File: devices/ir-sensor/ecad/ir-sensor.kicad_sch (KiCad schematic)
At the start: 5 parts, among them J1 SM03B-SRSS-TB, U1 EE-SY1201

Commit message: Panelizes the IR Sensors
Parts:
- C1: MPN (none) -> CL10B103KB8NNNC; Manufacturer (none) -> Samsung Electro-Mechanics
- J1: MPN (none) -> SM03B-SRSS-TB; Manufacturer (none) -> JST
- R1: MPN (none) -> RC0603FR-07100L; Manufacturer (none) -> YAGEO
- R2: MPN (none) -> RC0603FR-07220L; Manufacturer (none) -> YAGEO
- U1: Manufacturer (none) -> Omron Electronics Inc
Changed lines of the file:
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@@
+			)
+		)
+		(property "MPN" "CL10B103KB8NNNC"
+			(at 60.96 35.56 0)
+			(effects
+				(font
+					(size 1.27 1.27)
+				)
+				(hide yes)
+			)
+		)
+		(property "Manufacturer" "Samsung Electro-Mechanics"
+			(at 60.96 35.56 0)
+			(effects
+				(font
+					(size 1.27 1.27)
+				)
+				(hide yes)
 			)
 		)
@@
 			)
 		)
+		(property "Manufacturer" "Omron Electronics Inc"
+			(at 45.72 49.53 0)
+			(effects
+				(font
+					(size 1.27 1.27)
+				)
+				(hide yes)
+			)
+		)
 		(pin "1"
 		)
@@
 			)
 		)
+		(property "MPN" "RC0603FR-07100L"
+			(at 31.75 40.64 0)
+			(effects
+				(font
+					(size 1.27 1.27)
+				)
+				(hide yes)
+			)
+		)
+		(property "Manufacturer" "YAGEO"
+			(at 31.75 40.64 0)
+			(effects
+				(font
+					(size 1.27 1.27)
+				)
+				(hide yes)
+			)
+		)
 		(pin "1"
 		)
@@
 			)
 		)
+		(property "MPN" "SM03B-SRSS-TB"
+			(at 134.62 46.99 0)
+			(effects
+				(font
+					(size 1.27 1.27)
+				)
+				(hide yes)
+			)
+		)
+		(property "Manufacturer" "JST"
+			(at 134.62 46.99 0)
+			(effects
+				(font
+					(size 1.27 1.27)
+				)
+				(hide yes)
+			)
+		)
 		(pin "2"
 		)
@@
 			(at 71.12 46.99 0)
 			(effects
+				(font
+					(size 1.27 1.27)
+				)
+				(hide yes)
+			)
+		)
+		(property "MPN" "RC0603FR-07220L"
+			(at 71.12 46.99 0)
+			(effects
+				(font
+					(size 1.27 1.27)
+				)
+				(hide yes)
+			)
+		)
+		(property "Manufacturer" "YAGEO"
+			(at 71.12 46.99 0)
+			(effects

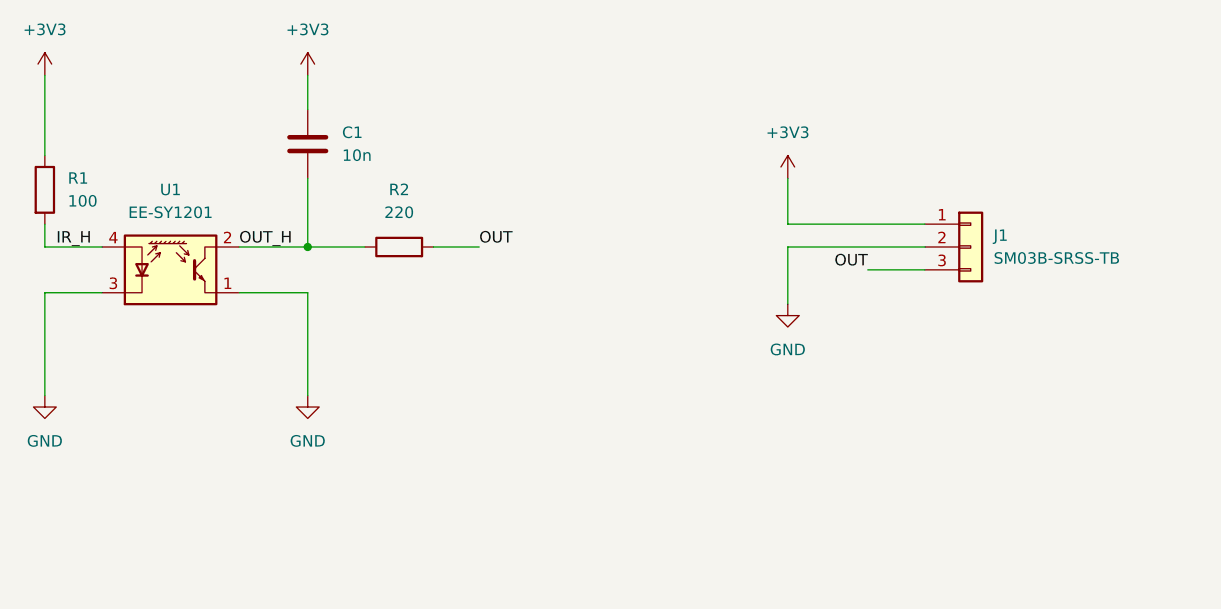
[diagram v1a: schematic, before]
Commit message: Adds license and output for IR Sensor
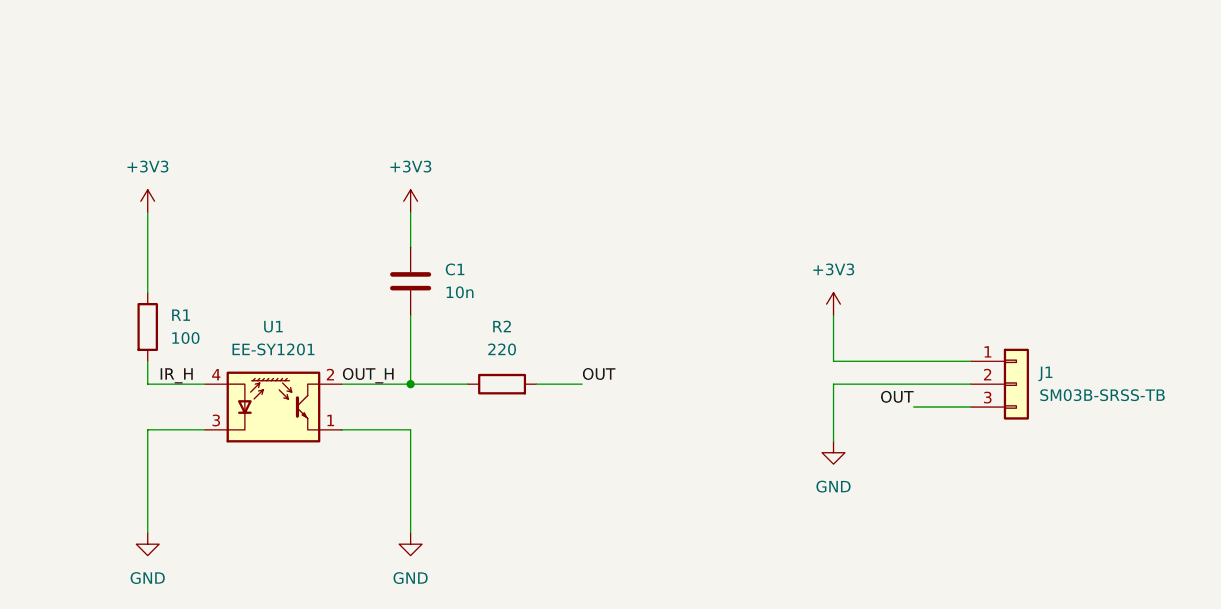
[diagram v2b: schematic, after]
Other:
- company: (none) -> Universitée de Lausanne
- title: (none) -> ZACI - IR Reflective Sensor
- moved on the sheet: C1, J1, R1, R2, U1
